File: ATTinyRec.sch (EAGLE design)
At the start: 13 parts, among them M1 ELECTRET_MICROPHON-WM-62PC/62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, U2 USD-SOCKETUSD

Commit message: Routed
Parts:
- removed JP1: AVR_SPI_PRG_6TESTPOINTS, SparkFun-Connectors:AVR_SPI_PRG_6TESTPOINTS
- added U$2: AVR_MINI_PROGSMD, SparkFun-Connectors:AVR_MINI_PROGSMD
- C1, C2: device rcl:C-USC0805K -> rcl:C-USC0402
- G1: value SL-150-1/2AA/PR -> SL-340/P; device battery:SL-150-1/2AA/PR -> battery:SL-340/P
- L1: device rcl:L-USL2825P -> resistor:L-USL2012C
- R1: device resistor:R-US_M0805 -> rcl:R-US_R0402
- R2: value 976k -> 660k; device resistor:R-US_M0805 -> rcl:R-US_R0402
- R3: value 562k -> 309k; device resistor:R-US_M0805 -> rcl:R-US_R0402
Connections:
- removed net N$5: D1.C, JP1.2, R1.1, U1.AREF, U2.VCC
- net N$20: now also U$2.RST; no longer JP1.5
- net N$3: now also U$1.SW
- net N$4: now also U$2.GND; no longer JP1.6
- net N$6: now also U$2.MOSI; no longer JP1.4
- net N$7: now also U$2.MISO; no longer JP1.1
- net N$9: now also U$2.SCK; no longer JP1.3
- net NET': now also D1.C, R1.1, U$2.VCC, U1.AREF, U2.VCC

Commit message: Gerber and board ordering zip done
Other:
- note added: "1"
- note added: "TSR1 Schematic"
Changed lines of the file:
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@@
 <?xml version="1.0" encoding="utf-8"?>
 <!DOCTYPE eagle SYSTEM "eagle.dtd">
-<eagle version="6.5.0">
+<eagle version="7.1.0">
 <drawing>
 <settings>
@@
 <part name="D1" library="diode" deviceset="DIODE-" device="DO214AC"/>
 <part name="U$2" library="SparkFun-Connectors" deviceset="AVR_MINI_PROG" device="SMD"/>
+<part name="FRAME1" library="frames" deviceset="FRAME_A_L" device=""/>
 </parts>
 <sheets>
 <sheet>
 <plain>
+<text x="137.16" y="-25.4" size="1.778" layer="91">TSR1 Schematic</text>
+<text x="198.12" y="-22.86" size="1.778" layer="91">1</text>
 </plain>
 <instances>
@@
 <instance part="D1" gate="G$1" x="27.94" y="78.74"/>
 <instance part="U$2" gate="G$1" x="152.4" y="78.74"/>
+<instance part="FRAME1" gate="G$1" x="-73.66" y="-35.56"/>
+<instance part="FRAME1" gate="G$2" x="99.06" y="-35.56"/>
 </instances>
 <busses>

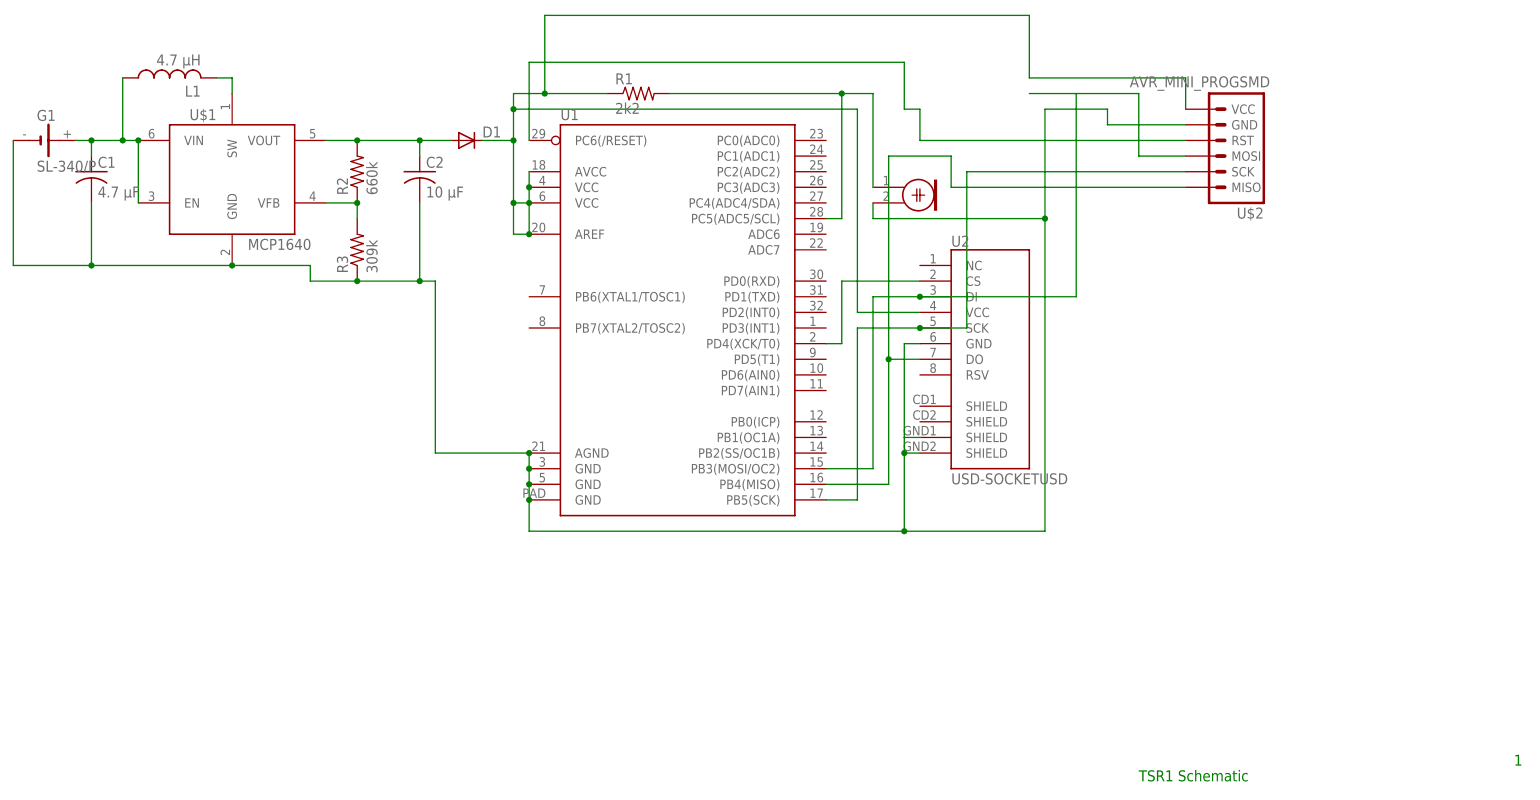
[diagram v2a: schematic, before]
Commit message: remade board and schematic consistent
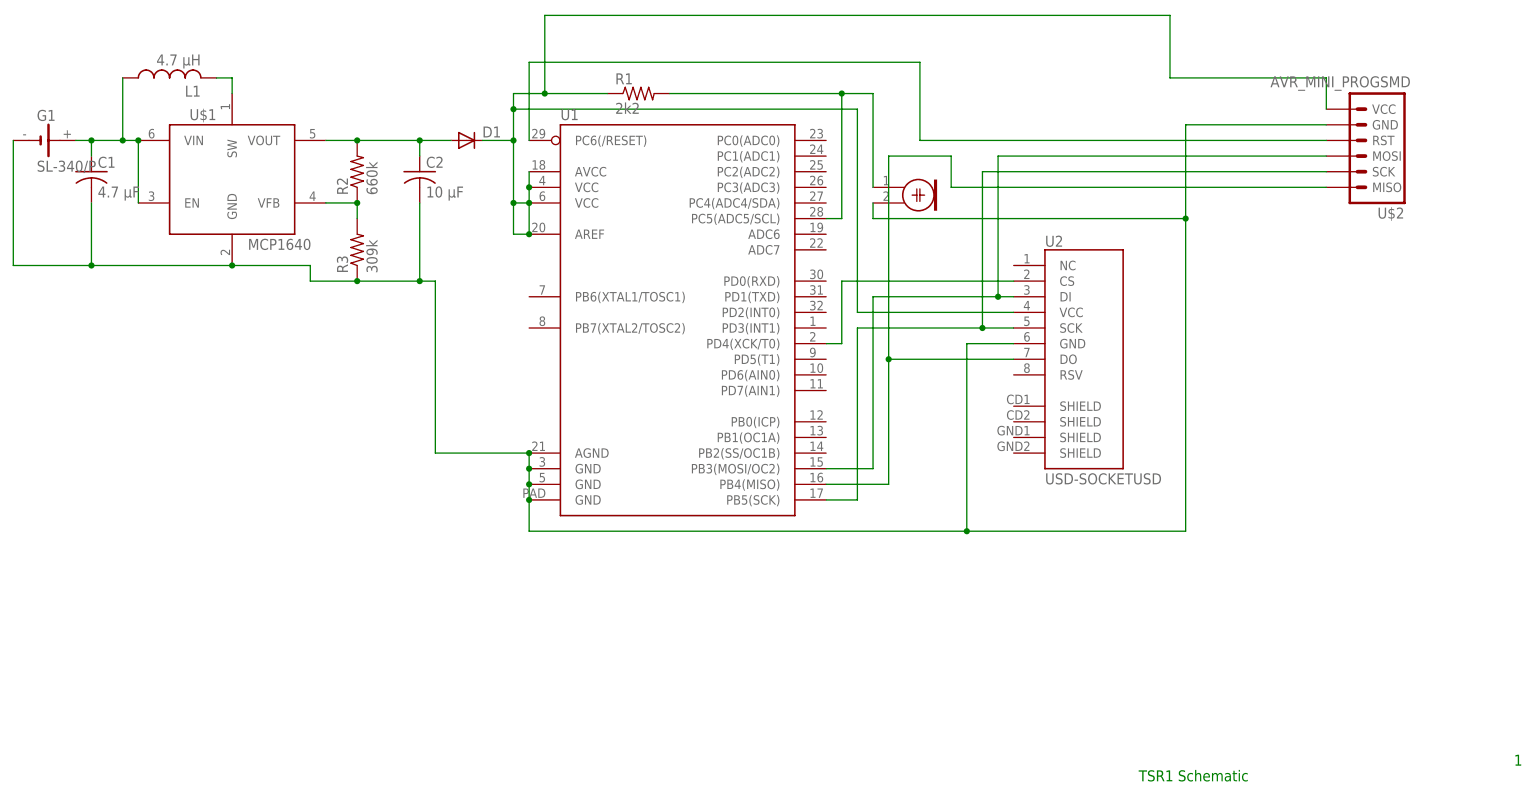
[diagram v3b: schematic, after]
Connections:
- net N$4: no longer U2.SHIELD@3, U2.SHIELD@4
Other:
- moved on the sheet: U$2, U2
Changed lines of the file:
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@@
 <?xml version="1.0" encoding="utf-8"?>
 <!DOCTYPE eagle SYSTEM "eagle.dtd">
-<eagle version="7.1.0">
+<eagle version="6.6.0">
 <drawing>
 <settings>
@@
 <instances>
 <instance part="M1" gate="G$1" x="99.06" y="71.12"/>
-<instance part="U2" gate="G$1" x="109.22" y="45.72"/>
+<instance part="U2" gate="G$1" x="124.46" y="45.72"/>
 <instance part="L1" gate="G$1" x="-20.32" y="88.9" rot="R90"/>
 <instance part="G1" gate="G$1" x="-40.64" y="78.74"/>
@@
 <instance part="C2" gate="G$1" x="20.32" y="73.66"/>
 <instance part="D1" gate="G$1" x="27.94" y="78.74"/>
-<instance part="U$2" gate="G$1" x="152.4" y="78.74"/>
+<instance part="U$2" gate="G$1" x="175.26" y="78.74"/>
 <instance part="FRAME1" gate="G$1" x="-73.66" y="-35.56"/>
 <instance part="FRAME1" gate="G$2" x="99.06" y="-35.56"/>
@@
 <wire x1="93.98" y1="25.4" x2="93.98" y2="53.34" width="0.1524" layer="91"/>
 <pinref part="U2" gate="G$1" pin="DI"/>
-<wire x1="93.98" y1="53.34" x2="101.6" y2="53.34" width="0.1524" layer="91"/>
-<wire x1="119.38" y1="86.36" x2="127" y2="86.36" width="0.1524" layer="91"/>
-<wire x1="127" y1="86.36" x2="127" y2="53.34" width="0.1524" layer="91"/>
-<wire x1="127" y1="53.34" x2="101.6" y2="53.34" width="0.1524" layer="91"/>
-<junction x="101.6" y="53.34"/>
-<wire x1="127" y1="86.36" x2="137.16" y2="86.36" width="0.1524" layer="91"/>
-<wire x1="137.16" y1="86.36" x2="137.16" y2="76.2" width="0.1524" layer="91"/>
+<wire x1="93.98" y1="53.34" x2="114.3" y2="53.34" width="0.1524" layer="91"/>
+<wire x1="114.3" y1="53.34" x2="116.84" y2="53.34" width="0.1524" layer="91"/>
 <pinref part="U$2" gate="G$1" pin="MOSI"/>
-<wire x1="137.16" y1="76.2" x2="144.78" y2="76.2" width="0.1524" layer="91"/>
+<wire x1="167.64" y1="76.2" x2="114.3" y2="76.2" width="0.1524" layer="91"/>
+<wire x1="114.3" y1="76.2" x2="114.3" y2="53.34" width="0.1524" layer="91"/>
+<junction x="114.3" y="53.34"/>
 </segment>
 </net>
@@
 <segment>
 <pinref part="U2" gate="G$1" pin="DO"/>
-<wire x1="101.6" y1="43.18" x2="96.52" y2="43.18" width="0.1524" layer="91"/>
+<wire x1="116.84" y1="43.18" x2="96.52" y2="43.18" width="0.1524" layer="91"/>
 <wire x1="96.52" y1="43.18" x2="96.52" y2="22.86" width="0.1524" layer="91"/>
 <pinref part="U1" gate="U$1" pin="PB4(MISO)"/>
@@
 <pinref part="U$2" gate="G$1" pin="MISO"/>
 <wire x1="96.52" y1="76.2" x2="96.52" y2="43.18" width="0.1524" layer="91"/>
-<wire x1="144.78" y1="71.12" x2="106.68" y2="71.12" width="0.1524" layer="91"/>
+<wire x1="167.64" y1="71.12" x2="106.68" y2="71.12" width="0.1524" layer="91"/>
 <wire x1="106.68" y1="71.12" x2="106.68" y2="76.2" width="0.1524" layer="91"/>
 <wire x1="106.68" y1="76.2" x2="96.52" y2="76.2" width="0.1524" layer="91"/>
@@
 <segment>
 <pinref part="U2" gate="G$1" pin="SCK"/>
-<wire x1="101.6" y1="48.26" x2="91.44" y2="48.26" width="0.1524" layer="91"/>
+<wire x1="116.84" y1="48.26" x2="111.76" y2="48.26" width="0.1524" layer="91"/>
+<wire x1="111.76" y1="48.26" x2="91.44" y2="48.26" width="0.1524" layer="91"/>
 <wire x1="91.44" y1="48.26" x2="91.44" y2="20.32" width="0.1524" layer="91"/>
 <pinref part="U1" gate="U$1" pin="PB5(SCK)"/>
 <wire x1="91.44" y1="20.32" x2="86.36" y2="20.32" width="0.1524" layer="91"/>
-<wire x1="109.22" y1="73.66" x2="109.22" y2="48.26" width="0.1524" layer="91"/>
-<wire x1="109.22" y1="48.26" x2="101.6" y2="48.26" width="0.1524" layer="91"/>
-<junction x="101.6" y="48.26"/>
 <pinref part="U$2" gate="G$1" pin="SCK"/>
-<wire x1="144.78" y1="73.66" x2="109.22" y2="73.66" width="0.1524" layer="91"/>
+<wire x1="167.64" y1="73.66" x2="111.76" y2="73.66" width="0.1524" layer="91"/>
+<wire x1="111.76" y1="73.66" x2="111.76" y2="48.26" width="0.1524" layer="91"/>
+<junction x="111.76" y="48.26"/>
 </segment>
 </net>
@@
 <wire x1="88.9" y1="45.72" x2="88.9" y2="55.88" width="0.1524" layer="91"/>
 <pinref part="U2" gate="G$1" pin="CS"/>
-<wire x1="88.9" y1="55.88" x2="101.6" y2="55.88" width="0.1524" layer="91"/>
+<wire x1="88.9" y1="55.88" x2="116.84" y2="55.88" width="0.1524" layer="91"/>
 </segment>
 </net>
@@
 <wire x1="35.56" y1="78.74" x2="35.56" y2="83.82" width="0.1524" layer="91"/>
 <wire x1="35.56" y1="83.82" x2="35.56" y2="86.36" width="0.1524" layer="91"/>
-<wire x1="101.6" y1="50.8" x2="91.44" y2="50.8" width="0.1524" layer="91"/>
+<wire x1="116.84" y1="50.8" x2="91.44" y2="50.8" width="0.1524" layer="91"/>
 <wire x1="91.44" y1="50.8" x2="91.44" y2="83.82" width="0.1524" layer="91"/>
 <wire x1="91.44" y1="83.82" x2="35.56" y2="83.82" width="0.1524" layer="91"/>
@@
 <wire x1="40.64" y1="86.36" x2="40.64" y2="99.06" width="0.1524" layer="91"/>
 <junction x="40.64" y="86.36"/>
-<wire x1="40.64" y1="99.06" x2="119.38" y2="99.06" width="0.1524" layer="91"/>
-<wire x1="119.38" y1="99.06" x2="119.38" y2="88.9" width="0.1524" layer="91"/>
+<wire x1="40.64" y1="99.06" x2="142.24" y2="99.06" width="0.1524" layer="91"/>
+<wire x1="142.24" y1="99.06" x2="142.24" y2="88.9" width="0.1524" layer="91"/>
 <pinref part="D1" gate="G$1" pin="C"/>
 <wire x1="30.48" y1="78.74" x2="35.56" y2="78.74" width="0.1524" layer="91"/>
 <junction x="35.56" y="78.74"/>
 <pinref part="U$2" gate="G$1" pin="VCC"/>
-<wire x1="119.38" y1="88.9" x2="144.78" y2="88.9" width="0.1524" layer="91"/>
-<wire x1="144.78" y1="88.9" x2="144.78" y2="83.82" width="0.1524" layer="91"/>
+<wire x1="142.24" y1="88.9" x2="167.64" y2="88.9" width="0.1524" layer="91"/>
+<wire x1="167.64" y1="88.9" x2="167.64" y2="83.82" width="0.1524" layer="91"/>
 <wire x1="35.56" y1="68.58" x2="38.1" y2="68.58" width="0.1524" layer="91"/>
 <wire x1="38.1" y1="68.58" x2="38.1" y2="63.5" width="0.1524" layer="91"/>
@@
 <pinref part="U1" gate="U$1" pin="PC6(/RESET)"/>
 <wire x1="38.1" y1="91.44" x2="38.1" y2="78.74" width="0.1524" layer="91"/>
-<wire x1="101.6" y1="83.82" x2="99.06" y2="83.82" width="0.1524" layer="91"/>
-<wire x1="99.06" y1="83.82" x2="99.06" y2="91.44" width="0.1524" layer="91"/>
-<wire x1="99.06" y1="91.44" x2="38.1" y2="91.44" width="0.1524" layer="91"/>
-<wire x1="101.6" y1="83.82" x2="101.6" y2="78.74" width="0.1524" layer="91"/>
+<wire x1="101.6" y1="78.74" x2="101.6" y2="91.44" width="0.1524" layer="91"/>
+<wire x1="101.6" y1="91.44" x2="38.1" y2="91.44" width="0.1524" layer="91"/>
 <pinref part="U$2" gate="G$1" pin="RST"/>
-<wire x1="101.6" y1="78.74" x2="144.78" y2="78.74" width="0.1524" layer="91"/>
+<wire x1="101.6" y1="78.74" x2="167.64" y2="78.74" width="0.1524" layer="91"/>
 </segment>
 </net>
@@
 <wire x1="2.54" y1="58.42" x2="2.54" y2="55.88" width="0.1524" layer="91"/>
 <junction x="-10.16" y="58.42"/>
-<pinref part="U2" gate="G$1" pin="GND"/>
-<wire x1="101.6" y1="45.72" x2="99.06" y2="45.72" width="0.1524" layer="91"/>
-<wire x1="99.06" y1="45.72" x2="99.06" y2="30.48" width="0.1524" layer="91"/>
-<pinref part="U2" gate="G$1" pin="SHIELD@3"/>
-<wire x1="101.6" y1="30.48" x2="99.06" y2="30.48" width="0.1524" layer="91"/>
-<wire x1="99.06" y1="30.48" x2="99.06" y2="27.94" width="0.1524" layer="91"/>
-<pinref part="U2" gate="G$1" pin="SHIELD@4"/>
-<wire x1="99.06" y1="27.94" x2="101.6" y2="27.94" width="0.1524" layer="91"/>
-<wire x1="99.06" y1="27.94" x2="99.06" y2="15.24" width="0.1524" layer="91"/>
-<junction x="99.06" y="27.94"/>
 <pinref part="U1" gate="U$1" pin="GND@PAD"/>
 <pinref part="U1" gate="U$1" pin="GND@5"/>
@@
 <wire x1="22.86" y1="27.94" x2="22.86" y2="55.88" width="0.1524" layer="91"/>
 <junction x="38.1" y="27.94"/>
-<wire x1="99.06" y1="15.24" x2="38.1" y2="15.24" width="0.1524" layer="91"/>
+<wire x1="144.78" y1="15.24" x2="109.22" y2="15.24" width="0.1524" layer="91"/>
+<wire x1="109.22" y1="15.24" x2="38.1" y2="15.24" width="0.1524" layer="91"/>
 <wire x1="38.1" y1="15.24" x2="38.1" y2="20.32" width="0.1524" layer="91"/>
 <junction x="38.1" y="20.32"/>
 <pinref part="M1" gate="G$1" pin="2"/>
 <wire x1="93.98" y1="68.58" x2="93.98" y2="66.04" width="0.1524" layer="91"/>
-<wire x1="93.98" y1="66.04" x2="121.92" y2="66.04" width="0.1524" layer="91"/>
-<wire x1="121.92" y1="66.04" x2="121.92" y2="15.24" width="0.1524" layer="91"/>
-<wire x1="121.92" y1="15.24" x2="99.06" y2="15.24" width="0.1524" layer="91"/>
-<junction x="99.06" y="15.24"/>
-<wire x1="121.92" y1="83.82" x2="121.92" y2="66.04" width="0.1524" layer="91"/>
-<junction x="121.92" y="66.04"/>
+<wire x1="93.98" y1="66.04" x2="144.78" y2="66.04" width="0.1524" layer="91"/>
+<wire x1="144.78" y1="66.04" x2="144.78" y2="15.24" width="0.1524" layer="91"/>
+<wire x1="144.78" y1="81.28" x2="144.78" y2="66.04" width="0.1524" layer="91"/>
+<junction x="144.78" y="66.04"/>
 <pinref part="R3" gate="G$1" pin="1"/>
 <wire x1="2.54" y1="55.88" x2="10.16" y2="55.88" width="0.1524" layer="91"/>
@@
 <wire x1="20.32" y1="68.58" x2="20.32" y2="55.88" width="0.1524" layer="91"/>
 <junction x="20.32" y="55.88"/>
-<wire x1="121.92" y1="83.82" x2="132.08" y2="83.82" width="0.1524" layer="91"/>
-<wire x1="132.08" y1="83.82" x2="132.08" y2="81.28" width="0.1524" layer="91"/>
 <pinref part="U$2" gate="G$1" pin="GND"/>
-<wire x1="132.08" y1="81.28" x2="144.78" y2="81.28" width="0.1524" layer="91"/>
-</segment>
-</net>
+<wire x1="144.78" y1="81.28" x2="167.64" y2="81.28" width="0.1524" layer="91"/>
+<pinref part="U2" gate="G$1" pin="GND"/>
+<wire x1="116.84" y1="45.72" x2="109.22" y2="45.72" width="0.1524" layer="91"/>
+<wire x1="109.22" y1="45.72" x2="109.22" y2="15.24" width="0.1524" layer="91"/>
+<junction x="109.22" y="15.24"/>
+</segment>
+</net>

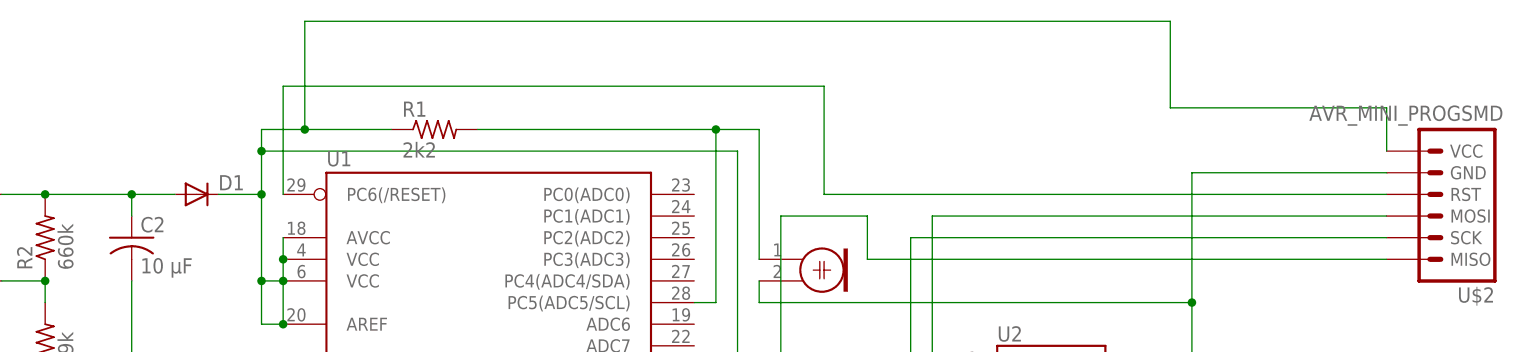
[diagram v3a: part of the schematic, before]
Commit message: added pullup resistor
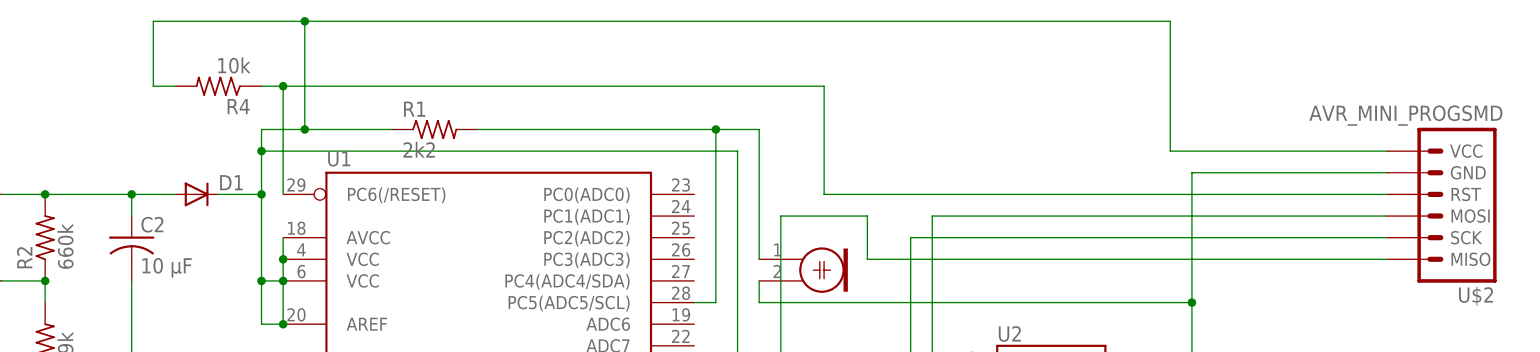
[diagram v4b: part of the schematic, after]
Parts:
- added R4: 10k, rcl:R-US_R0402
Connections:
- net N$4 renamed GND
- net N$6 renamed MOSI
- net N$7 renamed MISO
- net N$9 renamed SCK
- removed net N$20: U$2.RST, U1.PC6(/RESET)
- removed net NET': D1.C, R1.1, U$2.VCC, U1.AREF, U1.AVCC, U1.VCC@4, U1.VCC@6, U2.VCC
- new net RESET: R4.1, U$2.RST, U1.PC6(/RESET)
- new net VCC: D1.C, R1.1, R4.2, U$2.VCC, U1.AREF, U1.AVCC, U1.VCC@4, U1.VCC@6, U2.VCC
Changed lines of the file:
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@@
 <part name="U$2" library="SparkFun-Connectors" deviceset="AVR_MINI_PROG" device="SMD"/>
 <part name="FRAME1" library="frames" deviceset="FRAME_A_L" device=""/>
+<part name="R4" library="rcl" deviceset="R-US_" device="R0402" value="10k"/>
 </parts>
 <sheets>
@@
 <instance part="FRAME1" gate="G$1" x="-73.66" y="-35.56"/>
 <instance part="FRAME1" gate="G$2" x="99.06" y="-35.56"/>
+<instance part="R4" gate="G$1" x="30.48" y="91.44" rot="R180"/>
 </instances>
 <busses>
@@
 </segment>
 </net>
-<net name="N$6" class="0">
+<net name="MOSI" class="0">
 <segment>
 <pinref part="U1" gate="U$1" pin="PB3(MOSI/OC2)"/>
@@
 </segment>
 </net>
-<net name="N$7" class="0">
+<net name="MISO" class="0">
 <segment>
 <pinref part="U2" gate="G$1" pin="DO"/>
@@
 </segment>
 </net>
-<net name="N$9" class="0">
+<net name="SCK" class="0">
 <segment>
 <pinref part="U2" gate="G$1" pin="SCK"/>
@@
 </segment>
 </net>
-<net name="NET'" class="0">
+<net name="VCC" class="0">
 <segment>
 <pinref part="U1" gate="U$1" pin="VCC@6"/>
@@
 <junction x="40.64" y="86.36"/>
 <wire x1="40.64" y1="99.06" x2="142.24" y2="99.06" width="0.1524" layer="91"/>
-<wire x1="142.24" y1="99.06" x2="142.24" y2="88.9" width="0.1524" layer="91"/>
+<wire x1="142.24" y1="99.06" x2="142.24" y2="83.82" width="0.1524" layer="91"/>
 <pinref part="D1" gate="G$1" pin="C"/>
 <wire x1="30.48" y1="78.74" x2="35.56" y2="78.74" width="0.1524" layer="91"/>
 <junction x="35.56" y="78.74"/>
 <pinref part="U$2" gate="G$1" pin="VCC"/>
-<wire x1="142.24" y1="88.9" x2="167.64" y2="88.9" width="0.1524" layer="91"/>
-<wire x1="167.64" y1="88.9" x2="167.64" y2="83.82" width="0.1524" layer="91"/>
+<wire x1="142.24" y1="83.82" x2="167.64" y2="83.82" width="0.1524" layer="91"/>
 <wire x1="35.56" y1="68.58" x2="38.1" y2="68.58" width="0.1524" layer="91"/>
 <wire x1="38.1" y1="68.58" x2="38.1" y2="63.5" width="0.1524" layer="91"/>
 <junction x="35.56" y="68.58"/>
 <junction x="38.1" y="63.5"/>
+<pinref part="R4" gate="G$1" pin="2"/>
+<wire x1="25.4" y1="91.44" x2="22.86" y2="91.44" width="0.1524" layer="91"/>
+<wire x1="22.86" y1="91.44" x2="22.86" y2="99.06" width="0.1524" layer="91"/>
+<wire x1="22.86" y1="99.06" x2="40.64" y2="99.06" width="0.1524" layer="91"/>
+<junction x="40.64" y="99.06"/>
 </segment>
 </net>
-<net name="N$20" class="0">
+<net name="RESET" class="0">
 <segment>
 <pinref part="U1" gate="U$1" pin="PC6(/RESET)"/>
@@
 <pinref part="U$2" gate="G$1" pin="RST"/>
 <wire x1="101.6" y1="78.74" x2="167.64" y2="78.74" width="0.1524" layer="91"/>
+<pinref part="R4" gate="G$1" pin="1"/>
+<wire x1="38.1" y1="91.44" x2="35.56" y2="91.44" width="0.1524" layer="91"/>
+<junction x="38.1" y="91.44"/>
 </segment>
 </net>
@@
 </segment>
 </net>
-<net name="N$4" class="0">
+<net name="GND" class="0">
 <segment>
 <pinref part="G1" gate="G$1" pin="-"/>
